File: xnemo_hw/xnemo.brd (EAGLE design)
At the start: 38.6 x 29.8 mm, 34 parts, among them J1 MICRO_USB_B_RECEPT, J2 DM3D_MICRO_SD, J3 HEADER_2X5_0.05_SMD, J4 HEADER_2X5_0.05_THRU, J5 HEADER_2X5_0.05_THRU, U1 LTC3559, U2 L3GD20, U3 STM32F405RG, U5 HMC5883L, U6 ADXL345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

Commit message: r1 submitted
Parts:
- added C13: 2.2u, resistor:C0603
- added J6: (no value), pinhead:1X02
- moved C6 1.39 mm to (5.64, 28.3)
- moved L1 1.35 mm to (5.48, 25.6)
- moved C4 1.14 mm to (33.7, 9.84)
- moved C5 1.14 mm to (33.7, 13.0)
- moved X1 1.08 mm to (31.0, 11.4)
- moved C16 1.02 mm to (16.5, 19.3)
- moved C8 0.99 mm to (2.22, 25.2)
- moved J4 0.90 mm to (33.1, 22.7)
- moved J5 0.90 mm to (33.1, 6.19)
- moved C10 0.90 mm to (18.7, 20.5)
- moved C12 0.90 mm to (27.0, 25.7)
- moved C17 0.90 mm to (20.6, 28.7)
- moved U5 0.90 mm to (23.5, 4.13)
- moved C14 0.90 mm to (9.21, 21.3)
- moved J2 0.90 mm to (13.3, 6.35)
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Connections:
- removed net N$1: J5.P$4
- removed net N$16: J5.P$7
- removed net N$17: J5.P$5
- removed net N$2: J5.P$2
- removed net N$3: J5.P$3
- removed net N$4: J5.P$1
- removed net N$5: J5.P$6
- removed net N$6: J5.P$8
- removed net N$7: J4.P$9
- removed net N$8: J5.P$10
- removed net N$9: J5.P$9
- new net PA10: U3.P$43
- new net PB12: J5.P$9, U3.P$33
- new net PB13: J5.P$10, U3.P$34
- new net PB14: J5.P$4, U3.P$35
- new net PB15: J5.P$6, U3.P$36
- new net PC13: J5.P$1, U3.P$2
- new net UC_VBAT: C13.2, U3.P$1
- net 3V3: now also C13.1, J5.P$2, J5.P$8
- net GND: now also J5.P$3, J5.P$5, J5.P$7, J6.1
- net GYR_DRDY: now also U3.P$38; no longer U3.P$34
- net GYR_INT1: now also U3.P$37; no longer U3.P$33
- net I2C_SCL: now also J4.P$5
- net I2C_SDA: now also J4.P$9
- net PA1: no longer J4.P$5
- net SPI_CS_GYR: now also U3.P$41; no longer U3.P$35
- net VBAT: now also J6.2
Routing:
- net 3V3: track 144.7 -> 191.3 mm, vias 11 -> 12
- net PB12: track 0.00 -> 33.1 mm, vias 0 -> 6
- net I2C_SCL: track 5.76 -> 38.9 mm, vias 1 -> 3
- net PB13: track 0.00 -> 30.6 mm, vias 0 -> 1
- net PB15: track 0.00 -> 29.3 mm, vias 0 -> 1
- net I2C_SDA: track 5.10 -> 32.7 mm, vias 1 -> 2
- net PB14: track 0.00 -> 26.4 mm, vias 0 -> 1
- net VBAT: track 13.6 -> 20.6 mm
- net PC13: track 0.00 -> 4.57 mm
- net SD_CLK: track 14.2 -> 18.7 mm
- net UC_VBAT: track 0.00 -> 4.19 mm, vias 0 -> 1
- net RESET: track 23.9 -> 27.5 mm
- net SPI_CS_GYR: track 14.4 -> 17.6 mm
- net PC4: track 18.8 -> 20.9 mm
- net GND: track 22.9 -> 24.8 mm, vias 34 -> 45
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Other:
- board size 38.6 x 29.8 mm -> 39.8 x 31.3 mm
- board text added: "bnahill@gmail.com"
- board text added: "xNEMO r1"

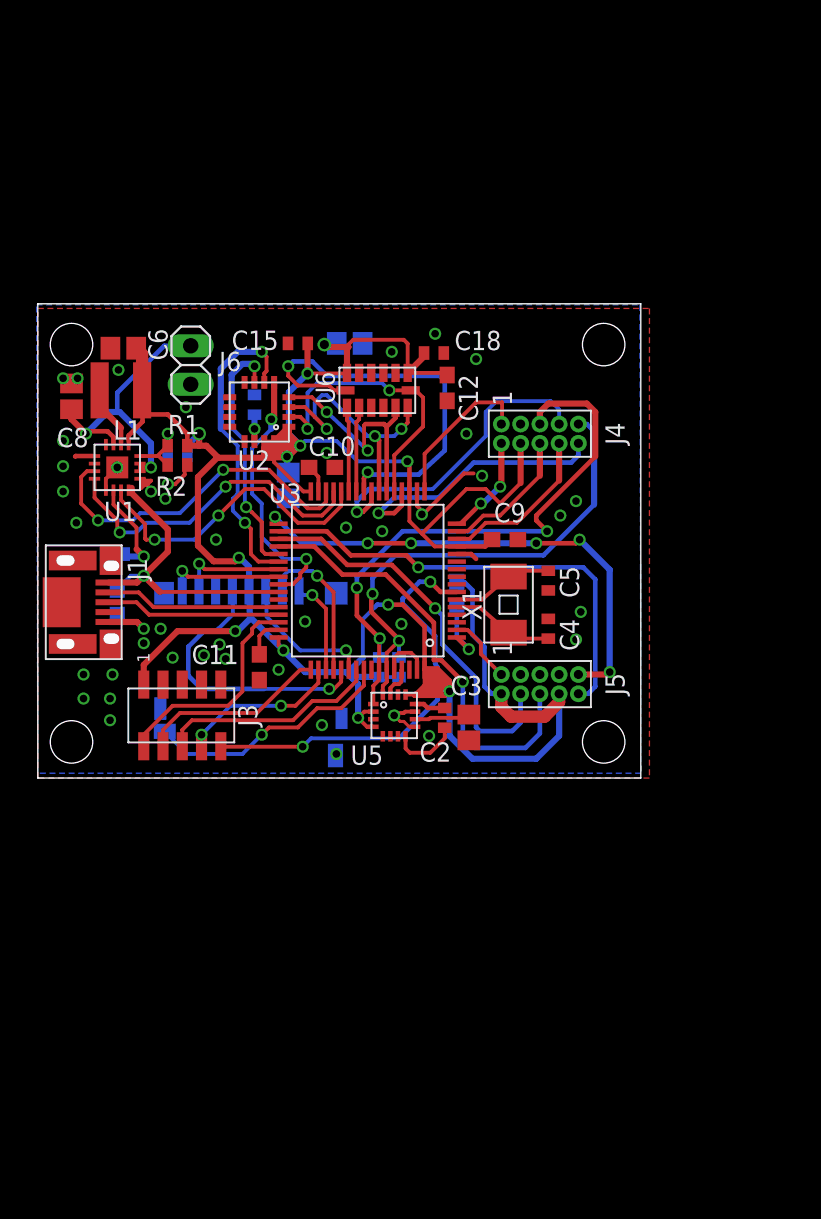
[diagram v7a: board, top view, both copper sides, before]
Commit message: Started conversion to larger PCB using LQFP100
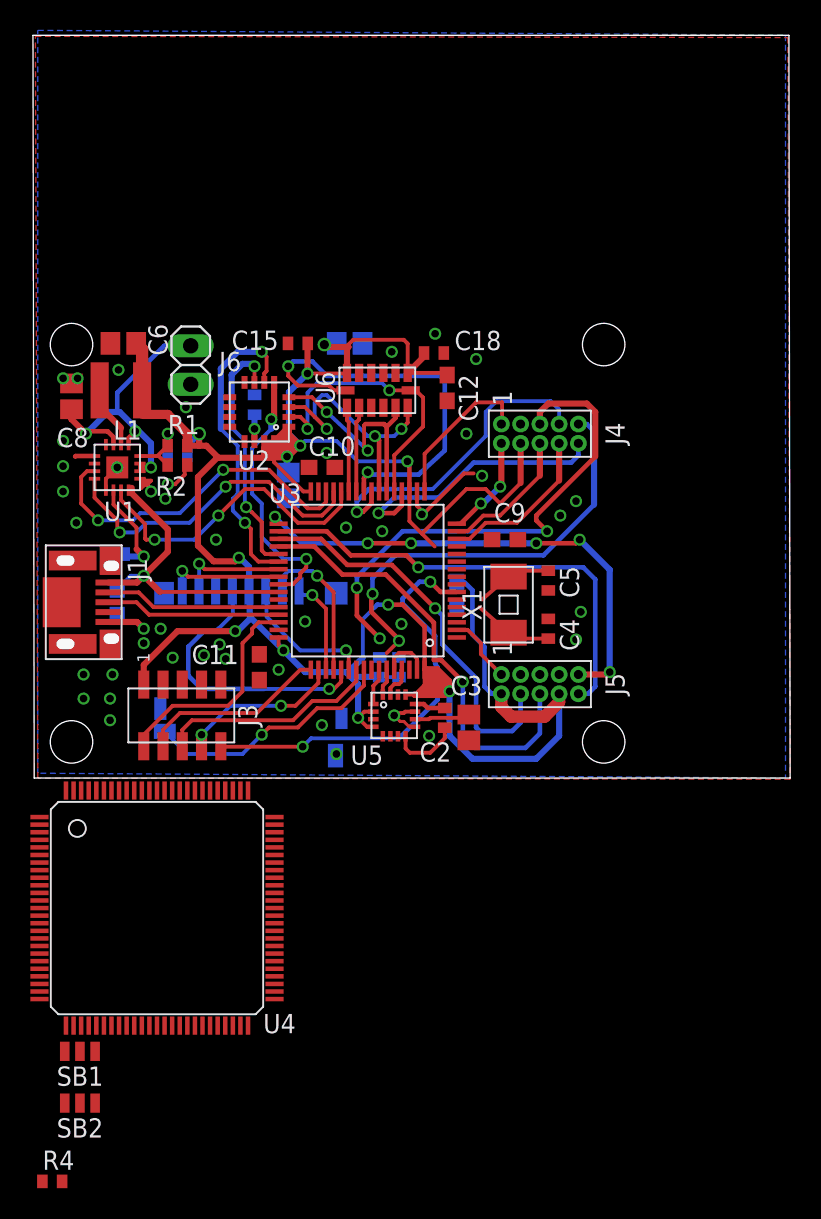
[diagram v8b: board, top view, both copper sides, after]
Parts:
- added R4: 22k, resistor:R0402
- added SB1, SB2: SOLDER_BRIDGE_2, xnemo:SOLDER_BRIDGE_2
- added U4: STM32F407VE, xnemo:ST_LQFP100
- C14: value 22p -> 10p
- C15: value 220n -> 0.22u
- C18: value 100n -> 0.1u
- R1: value (none) -> 68k
- R2: value (none) -> 22k
- moved C6 0.32 mm to (5.64, 28.7)
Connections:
- removed net UC_VBAT: C13.2, U3.P$1
- new net BOOT0: R4.1, U4.P$94
- new net N$1: SB1.P$2, U4.P$99
- new net N$10: U4.P$62
- new net N$11: U4.P$61
- new net N$12: U4.P$60
- new net N$13: U4.P$59
- new net N$14: U4.P$58
- new net N$15: U4.P$57
- new net N$16: U4.P$56
- new net N$17: U4.P$55
- new net N$18: U4.P$54
- new net N$19: U4.P$53
- new net N$2: U4.P$96
- new net N$20: U4.P$52
- new net N$21: U4.P$51
- new net N$22: U4.P$72
- new net N$24: U4.P$75
- new net N$25: U4.P$76
- new net N$26: U4.P$77
- new net N$27: U4.P$78
- new net N$28: U4.P$79
- new net N$29: U4.P$80
- new net N$3: U4.P$69
- new net N$30: U4.P$81
- new net N$31: U4.P$82
- new net N$32: U4.P$83
- new net N$33: U4.P$84
- new net N$34: U4.P$85
- new net N$35: U4.P$86
- new net N$36: U4.P$87
- new net N$37: U4.P$88
- new net N$38: U4.P$89
- new net N$39: U4.P$90
- new net N$4: U4.P$68
- new net N$40: U4.P$91
- new net N$44: U4.P$95
- new net N$45: U4.P$97
- new net N$46: U4.P$98
- new net N$47: U4.P$1
- new net N$48: U4.P$2
- new net N$49: U4.P$3
- new net N$5: U4.P$67
- new net N$50: U4.P$4
- new net N$51: U4.P$5
- new net N$53: U4.P$7
- new net N$54: U4.P$8
- new net N$55: U4.P$9
- new net N$56: U4.P$10
- new net N$57: U4.P$11
- new net N$58: U4.P$15
- new net N$59: U4.P$16
- new net N$6: U4.P$66
- new net N$60: U4.P$17
- new net N$61: U4.P$18
- new net N$62: SB2.P$2, U4.P$19
- new net N$63: U4.P$20
- new net N$66: U4.P$23
- new net N$67: U4.P$24
- new net N$68: U4.P$25
- new net N$69: U4.P$26
- new net N$7: U4.P$65
- new net N$70: U4.P$27
- new net N$71: U4.P$28
- new net N$72: U4.P$29
- new net N$73: U4.P$30
- new net N$74: U4.P$31
- new net N$75: U4.P$32
- new net N$76: U4.P$33
- new net N$77: U4.P$34
- new net N$78: U4.P$35
- new net N$79: U4.P$36
- new net N$8: U4.P$64
- new net N$80: U4.P$37
- new net N$81: U4.P$38
- new net N$82: U4.P$39
- new net N$83: U4.P$40
- new net N$84: U4.P$41
- new net N$85: U4.P$42
- new net N$86: U4.P$43
- new net N$87: U4.P$44
- new net N$88: U4.P$45
- new net N$89: U4.P$46
- new net N$9: U4.P$63
- new net N$90: U4.P$47
- new net N$91: U4.P$48
- new net N$93: U4.P$50
- net 3V3: now also C13.2, C9.1, SB1.P$1, SB2.P$1, U4.P$100, U4.P$21, U4.P$22, U4.P$6; no longer C13.1, C9.2, U1.P$5, U3.P$13
- net GND: now also C13.1, C9.2, R4.2, SB1.P$3, SB2.P$3, U4.P$74; no longer C9.1, U3.P$12
- net I2C_SCL: now also U4.P$92; no longer U3.P$58
- net I2C_SDA: now also U4.P$93; no longer U3.P$59
- net OSC_IN: now also U4.P$12; no longer U3.P$5
- net OSC_OUT: now also U4.P$13; no longer U3.P$6
- net RESET: now also U4.P$14
- net USB_D+: now also U4.P$71
- net USB_D-: now also U4.P$70
- net VBAT: now also U1.P$5
- net VCAP_1: now also U4.P$49; no longer U3.P$31
- net VCAP_2: now also U4.P$73; no longer U3.P$47
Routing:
- net 3V3: track 191.3 -> 184.8 mm
- net UC_VBAT: track 4.19 -> 0.00 mm, vias 1 -> 0
- net I2C_SCL: track 38.9 -> 34.9 mm
- net VCAP_2: track 2.87 -> 0.00 mm
- net I2C_SDA: track 32.7 -> 30.5 mm
- net VCAP_1: track 1.84 -> 0.00 mm
- net OSC_OUT: track 6.86 -> 5.20 mm
- net OSC_IN: track 6.93 -> 5.45 mm
- net GND: track 24.8 -> 23.4 mm
- net VBAT: track 20.6 -> 21.9 mm, vias 2 -> 3
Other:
- board size 39.8 x 31.3 mm -> 49.9 x 49 mm
